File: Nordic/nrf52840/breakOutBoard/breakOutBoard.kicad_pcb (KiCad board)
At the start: 4 copper layers, 30 x 26.8 mm, 24 parts, among them J1 Conn_ARM_JTAG_SWD_10, U1 NRF52840-QFAA-R7, Y1 Crystal, Y2 ECS-327MVATX-3-CN-TR3

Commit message: projects
Update projects
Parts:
- C10, C11, C12, C13, C9: moved to B.Cu
- Y1: value Crystal -> ECS-320-8-37B-CKY-TR; footprint Crystal:Crystal_SMD_Qantek_QC5CB-2Pin_5x3.2mm -> User_Footprint:XTAL_ECS-160-9-37-CKM-TR
- moved J1 10.1 mm to (170.8, 90.7), turned to 180 degrees
- moved C9 5.84 mm to (155.1, 81.6), turned to 0 degrees
- moved Y1 4.69 mm to (154.9, 79.8), turned to 0 degrees
- moved C12 3.90 mm to (159.3, 79.3), turned to 90 degrees
- moved C10 3.18 mm to (155.5, 77.5), turned to -90 degrees
- moved C11 2.98 mm to (160.6, 79.4), turned to 90 degrees
- moved J2 2.56 mm to (157.9, 81.0)
- moved C14 2.28 mm to (161.4, 82.0)
- moved C15 2.28 mm to (165.2, 82.0)
- moved L1 2.28 mm to (163.3, 81.4)
- moved L2 2.28 mm to (167.0, 81.4)
- moved C4 1.60 mm to (149.7, 77.3), turned to 180 degrees
- moved C5 1.13 mm to (153.8, 74.2), turned to -90 degrees
- moved C6 1.09 mm to (155.1, 74.2), turned to -90 degrees
- moved C17 1.07 mm to (158.3, 85.7)
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- renumbered C18 to J2
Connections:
- C10 pad 1: Net-(U1-XC2) -> GND
- C10 pad 2: GND -> /XC1
- C9 pad 1: Net-(U1-XC1) -> GND
- C9 pad 2: GND -> /XC2
- J2 pad 1: unconnected-(C18-Pad1) -> VDD
- J2 pad 10: unconnected-(C18-Pad10) -> /P0.12
- J2 pad 11: unconnected-(C18-Pad11) -> /P1.09
- J2 pad 12: unconnected-(C18-Pad12) -> /P0.13
- J2 pad 13: unconnected-(C18-Pad13) -> /P0.11
- J2 pad 14: unconnected-(C18-Pad14) -> /P0.14
- J2 pad 15: unconnected-(C18-Pad15) -> /P0.17
- J2 pad 16: unconnected-(C18-Pad16) -> /P0.18
- J2 pad 17: unconnected-(C18-Pad17) -> /P0.19
- J2 pad 18: unconnected-(C18-Pad18) -> /P0.29
- J2 pad 19: unconnected-(C18-Pad19) -> /P0.20
- J2 pad 2: unconnected-(C18-Pad2) -> GND
- J2 pad 20: unconnected-(C18-Pad20) -> /P0.30
- J2 pad 21: unconnected-(C18-Pad21) -> /P0.21
- J2 pad 22: unconnected-(C18-Pad22) -> /P0.31
- J2 pad 23: unconnected-(C18-Pad23) -> /P0.22
- J2 pad 24: unconnected-(C18-Pad24) -> /P0.03
- J2 pad 25: unconnected-(C18-Pad25) -> /P0.23
- J2 pad 26: unconnected-(C18-Pad26) -> /P0.02
- J2 pad 27: unconnected-(C18-Pad27) -> /P0.24
- J2 pad 28: unconnected-(C18-Pad28) -> /P0.28
- J2 pad 29: unconnected-(C18-Pad29) -> /P1.00
- J2 pad 3: unconnected-(C18-Pad3) -> VDD
- J2 pad 30: unconnected-(C18-Pad30) -> /P1.15
- J2 pad 31: unconnected-(C18-Pad31) -> /P0.09
- J2 pad 32: unconnected-(C18-Pad32) -> /P0.09
- J2 pad 4: unconnected-(C18-Pad4) -> GND
- J2 pad 5: unconnected-(C18-Pad5) -> /P0.04
- J2 pad 6: unconnected-(C18-Pad6) -> /P0.08
- J2 pad 7: unconnected-(C18-Pad7) -> /P0.05
- J2 pad 8: unconnected-(C18-Pad8) -> /P1.08
- J2 pad 9: unconnected-(C18-Pad9) -> /P0.07
- U1 pad 35: Net-(U1-XC1) -> /XC2
- U1 pad 36: Net-(U1-XC2) -> /XC1
- Y1 pad 1: Net-(U1-XC2) -> /XC1
- Y1 pad 2: Net-(U1-XC1) -> GND
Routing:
- net GND: track 0.00 -> 50.1 mm, vias 0 -> 10
- net Net-(U1-DEC4): track 2.57 -> 37.3 mm, vias 0 -> 2
- net /P0.28: track 0.00 -> 32.4 mm, vias 0 -> 1
- net /P0.02: track 0.00 -> 30.1 mm, vias 0 -> 1
- net /P1.15: track 0.00 -> 27.0 mm, vias 0 -> 1
- net /P0.03: track 0.00 -> 26.7 mm, vias 0 -> 1
- net /P0.29: track 0.00 -> 25.5 mm, vias 0 -> 1
- net /P0.30: track 0.00 -> 23.6 mm, vias 0 -> 1
- net /P0.31: track 0.00 -> 21.0 mm, vias 0 -> 1
- net /P0.07: track 0.00 -> 18.0 mm
- net /P0.08: track 0.00 -> 16.8 mm, vias 0 -> 1
- net /P0.09: track 0.00 -> 16.3 mm, vias 0 -> 1
- net /P1.08: track 0.00 -> 15.7 mm, vias 0 -> 1
- net VDD: track 10.8 -> 26.0 mm, vias 1 -> 6
- net /P1.09: track 0.00 -> 15.1 mm
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- added copper zone on In1.Cu, net GND
- added copper zone on In2.Cu, net VDD

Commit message: antenna
Implementing antenna layout
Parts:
- added C3: 1.0pF, Capacitor_SMD:C_0402_1005Metric_Pad0.74x0.62mm_HandSolder, F.Cu at (170.2, 83.2)
- added E1: 2450AT18A0100001E, User_Footprint:XCVR_2450AT18A0100001E, F.Cu at (165.5, 72.7)
- added L5: 2.7nH, Inductor_SMD:L_0402_1005Metric_Pad0.77x0.64mm_HandSolder, F.Cu at (166.1, 78.3)
- added L6: 3.9nH, Inductor_SMD:L_0402_1005Metric_Pad0.77x0.64mm_HandSolder, F.Cu at (165.5, 76.3)
- C14: value 1pF -> 1.0pF
- C15: value 1p2F -> 1.2pF
- L1: value 4n7H -> 4.7nH
- L2: value 2n2H -> 2.2nH
- moved J1 24.4 mm to (187.0, 72.4)
- moved C9 2.37 mm to (157.3, 82.4), turned to 90 degrees
- moved C13 1.96 mm to (150.7, 86.6)
- moved C15 1.80 mm to (163.4, 82.0)
- moved L2 1.80 mm to (165.2, 81.4)
- moved L1 1.63 mm to (161.7, 81.4)
- moved Y1 1.58 mm to (156.5, 79.9)
- moved C14 1.45 mm to (160.0, 82.0)
- moved C16 0.71 mm to (150.6, 86.7)
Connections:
- J2 pad 31: /P0.09 -> unconnected-(J2-Pad31)
- L2 pad 2: unconnected-(L2-Pad2) -> Net-(C3-Pad1)
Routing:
- net GND: track 50.1 -> 41.4 mm, vias 10 -> 24
- net /swdclk: track 16.8 -> 9.08 mm
- net /swdio: track 17.2 -> 9.81 mm
- net /P1.15: track 27.0 -> 31.3 mm
- net Net-(U1-DEC4): track 37.3 -> 41.3 mm
- net /P0.29: track 25.5 -> 28.9 mm
- net /P0.31: track 21.0 -> 24.1 mm
- net /P0.30: track 23.6 -> 26.5 mm
- net Net-(U1-ANT): track 5.25 -> 3.88 mm
- net /XC2: track 5.85 -> 4.72 mm
- net VDD: track 26.0 -> 27.0 mm
- net /P0.12: track 12.7 -> 13.6 mm
- net /P0.28: track 32.4 -> 31.7 mm

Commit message: layout
changed Layout
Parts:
- C1, C14, C15, C16, C17, C3, C4, C5, C6: footprint Capacitor_SMD:C_0402_1005Metric_Pad0.74x0.62mm_HandSolder -> Capacitor_SMD:C_0201_0603Metric
- C10, C11, C12, C13, C19, C2, C9: footprint Capacitor_SMD:C_0402_1005Metric_Pad0.74x0.62mm_HandSolder -> Capacitor_SMD:C_0201_0603Metric; moved to F.Cu
- L1, L2, L3, L4, L5, L6: footprint Inductor_SMD:L_0402_1005Metric_Pad0.77x0.64mm_HandSolder -> Inductor_SMD:L_0201_0603Metric
- Y1, Y2: moved to F.Cu
- moved J1 23.2 mm to (170.7, 89.0)
- moved C3 16.5 mm to (159.0, 71.1)
- moved C9 10.8 mm to (151.2, 73.5), turned to 45 degrees
- moved L2 10.1 mm to (156.9, 75.7), turned to 90 degrees
- moved C6 9.39 mm to (146.4, 77.7), turned to 135 degrees
- moved C15 9.23 mm to (156.0, 76.4), turned to 135 degrees
- moved L5 9.03 mm to (160.2, 71.5), turned to -90 degrees
- moved C5 8.26 mm to (147.1, 79.0), turned to 45 degrees
- moved C2 7.65 mm to (144.8, 88.8)
- moved Y2 7.54 mm to (145.2, 86.2), turned to 90 degrees
- moved L1 7.41 mm to (155.4, 77.6), turned to 45 degrees
- moved L4 7.34 mm to (145.8, 78.8), turned to -135 degrees
- moved C14 6.88 mm to (154.3, 78.2), turned to 135 degrees
- moved C11 6.67 mm to (154.5, 76.7), turned to 45 degrees
- moved Y1 6.66 mm to (152.3, 74.7), turned to 45 degrees
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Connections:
- J2 pad 18: /P0.29 -> /P0.31
- J2 pad 22: /P0.31 -> /P0.29
- J2 pad 24: /P0.03 -> /P0.28
- J2 pad 26: /P0.02 -> /P0.03
- J2 pad 28: /P0.28 -> unconnected-(J2-Pad28)
- J2 pad 31: unconnected-(J2-Pad31) -> /P0.10
- J2 pad 34: unconnected-(J2-Pad34) -> /P0.02
- J2 pad 43: unconnected-(J2-Pad43) -> VDD
- J2 pad 44: unconnected-(J2-Pad44) -> GND
- J2 pad 45: unconnected-(J2-Pad45) -> VDD
- J2 pad 46: unconnected-(J2-Pad46) -> GND
- J2 pad 47: unconnected-(J2-Pad47) -> VDD
- J2 pad 48: unconnected-(J2-Pad48) -> GND
- J2 pad 49: unconnected-(J2-Pad49) -> VDD
- J2 pad 50: unconnected-(J2-Pad50) -> GND
- J2 pad 51: unconnected-(J2-Pad51) -> VDD
- J2 pad 52: unconnected-(J2-Pad52) -> GND
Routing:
- net /P0.10: track 0.00 -> 23.4 mm
- net Net-(U1-DEC4): track 41.3 -> 23.8 mm
- net VDD: track 27.0 -> 39.2 mm, vias 6 -> 9
- net /swdclk: track 9.08 -> 18.4 mm, vias 0 -> 1
- net /swdio: track 9.81 -> 18.4 mm, vias 0 -> 1
- net /P0.04: track 19.5 -> 12.1 mm
- net /P1.15: track 31.3 -> 24.1 mm
- net GND: track 41.4 -> 48.3 mm, vias 24 -> 72
- net /P0.05: track 18.7 -> 12.0 mm
- net /P0.07: track 18.0 -> 11.9 mm
- net Net-(C3-Pad1): track 0.00 -> 5.83 mm
- net /P0.09: track 16.3 -> 22.1 mm
- net /P0.08: track 16.8 -> 11.6 mm
- net /P0.31: track 24.1 -> 28.7 mm
- net /P1.08: track 15.7 -> 11.1 mm
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- added copper zone on F.Cu, net GND
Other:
- board text added: "NRF52840 Breakout Board V1.0"
- board text added: "SWD Connector"

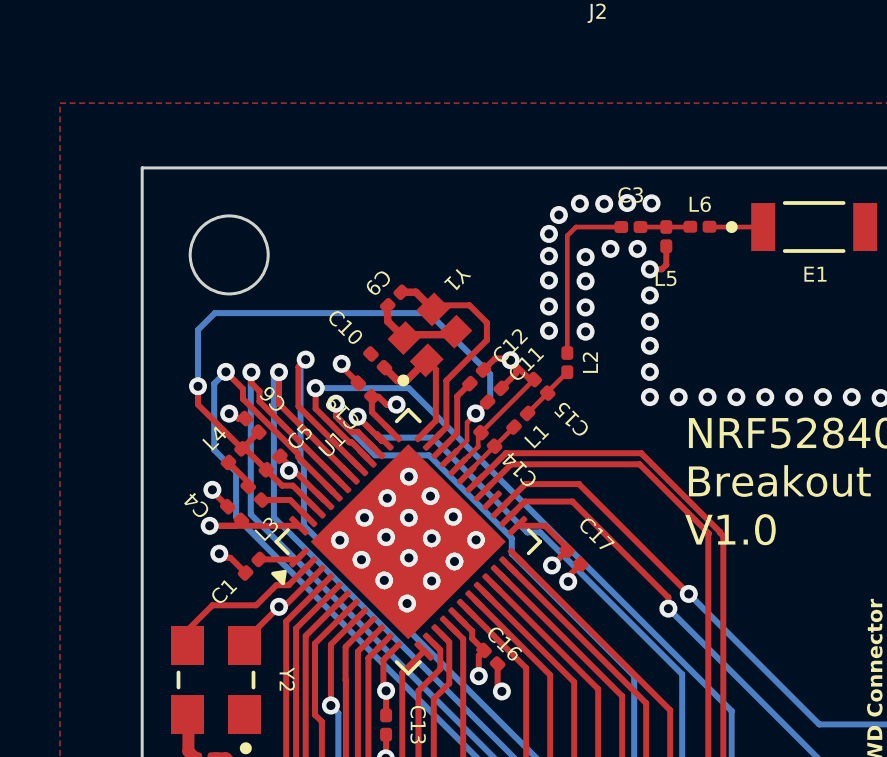
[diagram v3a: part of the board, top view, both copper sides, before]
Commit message: Update
Change some footprints and update RF trace
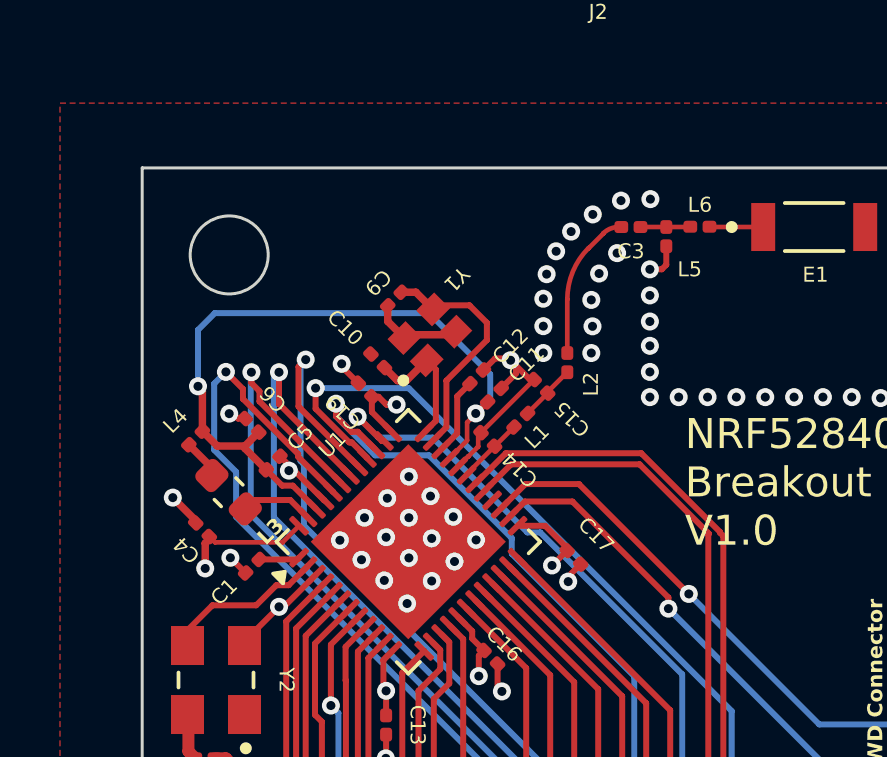
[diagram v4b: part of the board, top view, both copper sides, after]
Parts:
- C10, C9: value C -> 6pF
- C11: value C -> N/C
- C2: value 0u01F -> 0.01uF
- L3: footprint Inductor_SMD:L_0201_0603Metric -> Inductor_SMD:L_0603_1608Metric
- moved L4 1.45 mm to (144.5, 78.2)
- moved C4 1.20 mm to (144.8, 81.2)
- moved L3 0.88 mm to (145.6, 80.0)
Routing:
- net Net-(U1-DEC4): track 23.8 -> 25.3 mm
- net Net-(C3-Pad1): track 5.83 -> 5.03 mm
- net Net-(U1-DCC): track 1.76 -> 2.44 mm
- net GND: track 48.3 -> 48.2 mm, vias 72 -> 70
